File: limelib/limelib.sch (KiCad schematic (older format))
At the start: 6 parts, among them J1 ESC_CONN, SW1 SW_Push, U1 ATtiny85-20PU

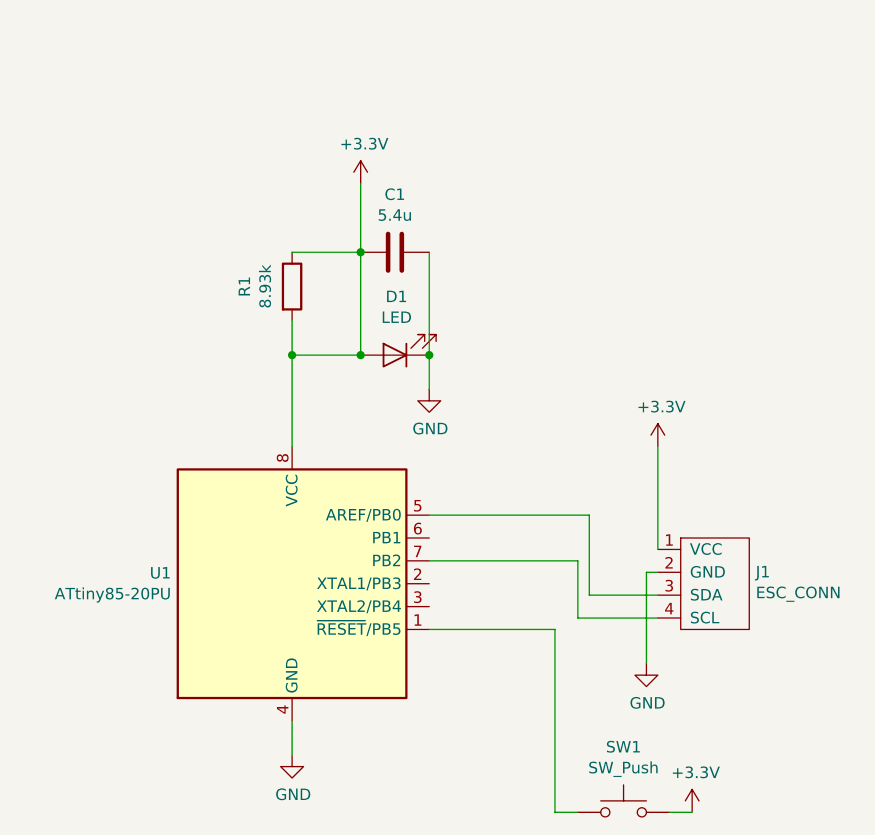
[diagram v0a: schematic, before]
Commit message: fix voltage regulator and switch
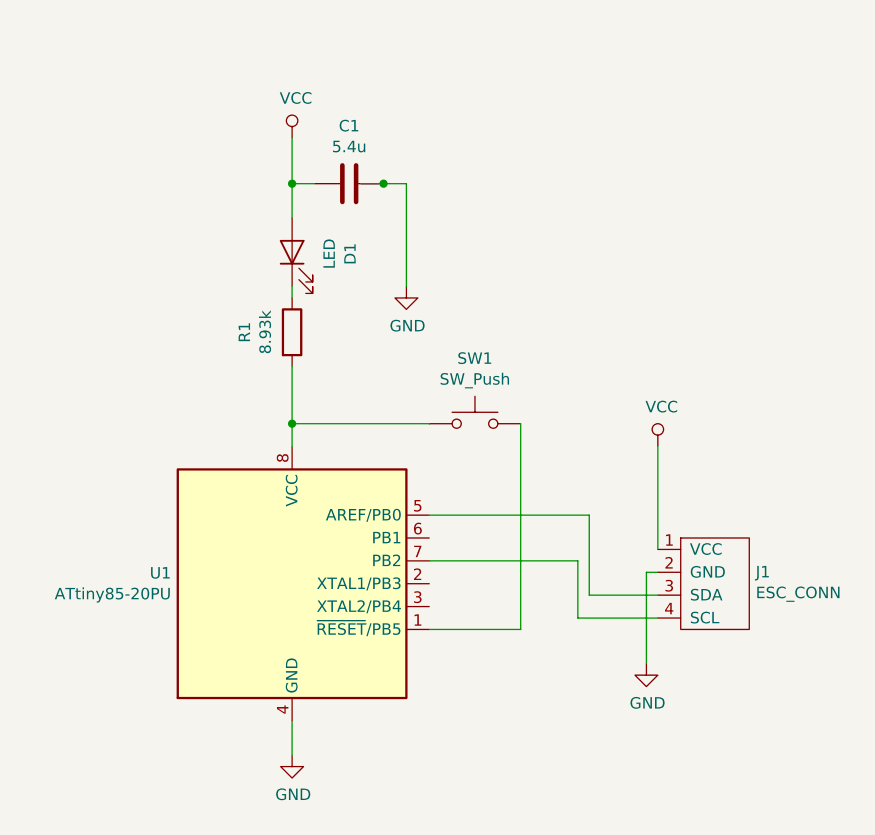
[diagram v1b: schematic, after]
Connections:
- net labels added: VCC
- net labels removed: +3.3V
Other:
- moved on the sheet: C1, D1, R1, SW1
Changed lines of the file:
@@
 EESchema Schematic File Version 4
+LIBS:limelib-cache
 EELAYER 30 0
 EELAYER END
@@
 L Device:R R1
 U 1 1 5DCA0E0D
-P 5650 2450
-F 0 "R1" V 5443 2450 50  0000 C CNN
-F 1 "8.93k" V 5534 2450 50  0000 C CNN
-F 2 "" V 5580 2450 50  0001 C CNN
-F 3 "~" H 5650 2450 50  0001 C CNN
-	1    5650 2450
+P 5650 2650
+F 0 "R1" V 5443 2650 50  0000 C CNN
+F 1 "8.93k" V 5534 2650 50  0000 C CNN
+F 2 "" V 5580 2650 50  0001 C CNN
+F 3 "~" H 5650 2650 50  0001 C CNN
+	1    5650 2650
 	1    0    0    -1
 $EndComp
@@
 L Device:C C1
 U 1 1 5DCA153E
-P 6100 2300
-F 0 "C1" V 6352 2300 50  0000 C CNN
-F 1 "5.4u" V 6261 2300 50  0000 C CNN
-F 2 "" H 6138 2150 50  0001 C CNN
-F 3 "~" H 6100 2300 50  0001 C CNN
-	1    6100 2300
+P 5900 2000
+F 0 "C1" V 6152 2000 50  0000 C CNN
+F 1 "5.4u" V 6061 2000 50  0000 C CNN
+F 2 "" H 5938 1850 50  0001 C CNN
+F 3 "~" H 5900 2000 50  0001 C CNN
+	1    5900 2000
 	0    -1   -1   0
 $EndComp
@@
 L Device:LED D1
 U 1 1 5DCA22B6
-P 6100 2750
-F 0 "D1" H 6093 2495 50  0000 C CNN
-F 1 "LED" H 6093 2586 50  0000 C CNN
-F 2 "" H 6100 2750 50  0001 C CNN
-F 3 "~" H 6100 2750 50  0001 C CNN
-	1    6100 2750
-	-1   0    0    1
+P 5650 2300
+F 0 "D1" H 5643 2045 50  0000 C CNN
+F 1 "LED" H 5643 2136 50  0000 C CNN
+F 2 "" H 5650 2300 50  0001 C CNN
+F 3 "~" H 5650 2300 50  0001 C CNN
+	1    5650 2300
+	0    -1   -1   0
 $EndComp
 $Comp
 L Switch:SW_Push SW1
 U 1 1 5DCA2F12
-P 7100 4750
-F 0 "SW1" H 7100 5035 50  0000 C CNN
-F 1 "SW_Push" H 7100 4944 50  0000 C CNN
-F 2 "" H 7100 4950 50  0001 C CNN
-F 3 "~" H 7100 4950 50  0001 C CNN
-	1    7100 4750
+P 6450 3050
+F 0 "SW1" H 6450 3335 50  0000 C CNN
+F 1 "SW_Push" H 6450 3244 50  0000 C CNN
+F 2 "" H 6450 3250 50  0001 C CNN
+F 3 "~" H 6450 3250 50  0001 C CNN
+	1    6450 3050
 	1    0    0    -1
 $EndComp
@@
 	7200 3700 7200 4100
 Wire Wire Line
-	6250 3950 6800 3950
-Wire Wire Line
-	6800 3950 6800 4750
-Wire Wire Line
-	6800 4750 6900 4750
-Wire Wire Line
-	7400 4750 7300 4750
-Wire Wire Line
 	7250 3800 6950 3800
 Wire Wire Line
@@
 L power:GND #PWR?
 U 1 1 5DCBD74A
-P 6250 2900
-F 0 "#PWR?" H 6250 2650 50  0001 C CNN
-F 1 "GND" H 6255 2727 50  0000 C CNN
-F 2 "" H 6250 2900 50  0001 C CNN
-F 3 "" H 6250 2900 50  0001 C CNN
-	1    6250 2900
+P 6150 2450
+F 0 "#PWR?" H 6150 2200 50  0001 C CNN
+F 1 "GND" H 6155 2277 50  0000 C CNN
+F 2 "" H 6150 2450 50  0001 C CNN
+F 3 "" H 6150 2450 50  0001 C CNN
+	1    6150 2450
 	1    0    0    -1
 $EndComp
 Wire Wire Line
-	5950 2300 5950 2000
-Connection ~ 5950 2300
+	7250 3150 7250 3600
+$Comp
+L power:VCC #PWR?
+U 1 1 5DCB2ABE
+P 5650 1800
+F 0 "#PWR?" H 5650 1650 50  0001 C CNN
+F 1 "VCC" H 5667 1973 50  0000 C CNN
+F 2 "" H 5650 1800 50  0001 C CNN
+F 3 "" H 5650 1800 50  0001 C CNN
+	1    5650 1800
+	1    0    0    -1
+$EndComp
 Wire Wire Line
-	5650 2600 5650 2750
+	5650 2450 5650 2500
 Wire Wire Line
-	5650 2300 5950 2300
+	5650 1800 5650 2000
+Connection ~ 5650 2000
 Wire Wire Line
-	5950 2750 5650 2750
+	5650 2000 5650 2150
 Wire Wire Line
-	5650 2750 5650 3150
-Connection ~ 5650 2750
+	6150 2000 6150 2450
+Wire Wire Line
+	5650 2000 5750 2000
+Wire Wire Line
+	5950 2000 6050 2000
 $Comp
-L power:+3.3V #PWR?
-U 1 1 5DCDEE7B
+L power:VCC #PWR?
+U 1 1 5DCBCC27
 P 7250 3150
 F 0 "#PWR?" H 7250 3000 50  0001 C CNN
-F 1 "+3.3V" H 7265 3323 50  0000 C CNN
+F 1 "VCC" H 7267 3323 50  0000 C CNN
 F 2 "" H 7250 3150 50  0001 C CNN
 F 3 "" H 7250 3150 50  0001 C CNN
@@
 	1    0    0    -1
 $EndComp
+Connection ~ 6050 2000
 Wire Wire Line
-	7250 3150 7250 3600
-$Comp
-L power:+3.3V #PWR?
-U 1 1 5DCDFD0C
-P 5950 2000
-F 0 "#PWR?" H 5950 1850 50  0001 C CNN
-F 1 "+3.3V" H 5965 2173 50  0000 C CNN
-F 2 "" H 5950 2000 50  0001 C CNN
-F 3 "" H 5950 2000 50  0001 C CNN
-	1    5950 2000
-	1    0    0    -1
-$EndComp
-$Comp
-L power:+3.3V #PWR?
-U 1 1 5DCE016F
-P 7400 4750
-F 0 "#PWR?" H 7400 4600 50  0001 C CNN
-F 1 "+3.3V" H 7415 4923 50  0000 C CNN
-F 2 "" H 7400 4750 50  0001 C CNN
-F 3 "" H 7400 4750 50  0001 C CNN
-	1    7400 4750
-	1    0    0    -1
-$EndComp
+	6050 2000 6150 2000
 Wire Wire Line
-	6250 2300 6250 2750
-Connection ~ 6250 2750
+	5650 2800 5650 3050
 Wire Wire Line
-	6250 2750 6250 2900
+	6250 3050 5650 3050
+Connection ~ 5650 3050
 Wire Wire Line
-	5950 2300 5950 2750
-Connection ~ 5950 2750
+	5650 3050 5650 3150
+Wire Wire Line
+	6650 3050 6650 3950
+Wire Wire Line
+	6650 3950 6250 3950
 $EndSCHEMATC

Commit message: another shot at the LED regulator circuit
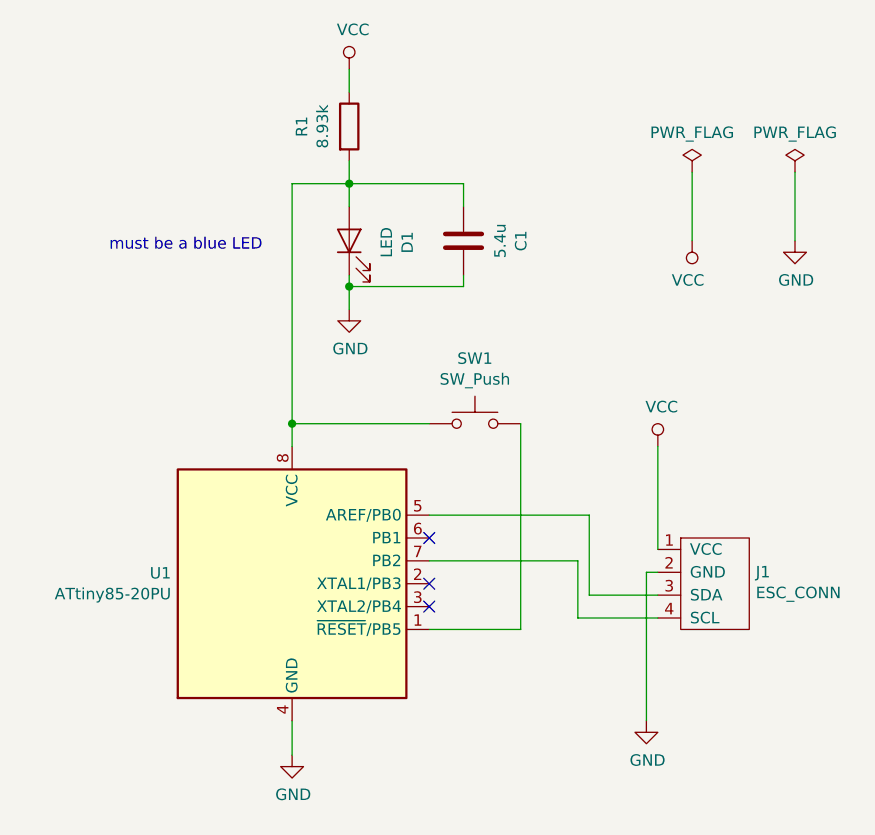
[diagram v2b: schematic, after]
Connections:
- wire segments 22 -> 27
- no-connect marks 0 -> 3
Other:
- note added: "must be a blue LED"
- moved on the sheet: C1, D1, R1
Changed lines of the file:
@@
 L Device:R R1
 U 1 1 5DCA0E0D
-P 5650 2650
-F 0 "R1" V 5443 2650 50  0000 C CNN
-F 1 "8.93k" V 5534 2650 50  0000 C CNN
-F 2 "" V 5580 2650 50  0001 C CNN
-F 3 "~" H 5650 2650 50  0001 C CNN
-	1    5650 2650
+P 5900 1750
+F 0 "R1" V 5693 1750 50  0000 C CNN
+F 1 "8.93k" V 5784 1750 50  0000 C CNN
+F 2 "" V 5830 1750 50  0001 C CNN
+F 3 "~" H 5900 1750 50  0001 C CNN
+	1    5900 1750
 	1    0    0    -1
 $EndComp
@@
 L Device:C C1
 U 1 1 5DCA153E
-P 5900 2000
-F 0 "C1" V 6152 2000 50  0000 C CNN
-F 1 "5.4u" V 6061 2000 50  0000 C CNN
-F 2 "" H 5938 1850 50  0001 C CNN
-F 3 "~" H 5900 2000 50  0001 C CNN
-	1    5900 2000
-	0    -1   -1   0
+P 6400 2250
+F 0 "C1" V 6652 2250 50  0000 C CNN
+F 1 "5.4u" V 6561 2250 50  0000 C CNN
+F 2 "" H 6438 2100 50  0001 C CNN
+F 3 "~" H 6400 2250 50  0001 C CNN
+	1    6400 2250
+	1    0    0    -1
 $EndComp
 $Comp
 L Device:LED D1
 U 1 1 5DCA22B6
-P 5650 2300
-F 0 "D1" H 5643 2045 50  0000 C CNN
-F 1 "LED" H 5643 2136 50  0000 C CNN
-F 2 "" H 5650 2300 50  0001 C CNN
-F 3 "~" H 5650 2300 50  0001 C CNN
-	1    5650 2300
+P 5900 2250
+F 0 "D1" H 5893 1995 50  0000 C CNN
+F 1 "LED" H 5893 2086 50  0000 C CNN
+F 2 "" H 5900 2250 50  0001 C CNN
+F 3 "~" H 5900 2250 50  0001 C CNN
+	1    5900 2250
 	0    -1   -1   0
 $EndComp
@@
 $EndComp
 $Comp
-L power:GND #PWR?
+L power:GND #PWR0101
 U 1 1 5DCA42A6
 P 5650 4500
-F 0 "#PWR?" H 5650 4250 50  0001 C CNN
+F 0 "#PWR0101" H 5650 4250 50  0001 C CNN
 F 1 "GND" H 5655 4327 50  0000 C CNN
 F 2 "" H 5650 4500 50  0001 C CNN
@@
 $EndComp
 $Comp
-L power:GND #PWR?
+L power:GND #PWR0102
 U 1 1 5DCADE5E
-P 7200 4100
-F 0 "#PWR?" H 7200 3850 50  0001 C CNN
-F 1 "GND" H 7205 3927 50  0000 C CNN
-F 2 "" H 7200 4100 50  0001 C CNN
-F 3 "" H 7200 4100 50  0001 C CNN
-	1    7200 4100
+P 7200 4350
+F 0 "#PWR0102" H 7200 4100 50  0001 C CNN
+F 1 "GND" H 7205 4177 50  0000 C CNN
+F 2 "" H 7200 4350 50  0001 C CNN
+F 3 "" H 7200 4350 50  0001 C CNN
+	1    7200 4350
 	1    0    0    -1
 $EndComp
@@
 	7250 3700 7200 3700
 Wire Wire Line
-	7200 3700 7200 4100
-Wire Wire Line
 	7250 3800 6950 3800
 Wire Wire Line
@@
 	6900 3650 6250 3650
 $Comp
-L power:GND #PWR?
-U 1 1 5DCBD74A
-P 6150 2450
-F 0 "#PWR?" H 6150 2200 50  0001 C CNN
-F 1 "GND" H 6155 2277 50  0000 C CNN
-F 2 "" H 6150 2450 50  0001 C CNN
-F 3 "" H 6150 2450 50  0001 C CNN
-	1    6150 2450
-	1    0    0    -1
-$EndComp
-Wire Wire Line
-	7250 3150 7250 3600
-$Comp
-L power:VCC #PWR?
+L power:VCC #PWR0104
 U 1 1 5DCB2ABE
-P 5650 1800
-F 0 "#PWR?" H 5650 1650 50  0001 C CNN
-F 1 "VCC" H 5667 1973 50  0000 C CNN
-F 2 "" H 5650 1800 50  0001 C CNN
-F 3 "" H 5650 1800 50  0001 C CNN
-	1    5650 1800
-	1    0    0    -1
-$EndComp
-Wire Wire Line
-	5650 2450 5650 2500
-Wire Wire Line
-	5650 1800 5650 2000
-Connection ~ 5650 2000
-Wire Wire Line
-	5650 2000 5650 2150
-Wire Wire Line
-	6150 2000 6150 2450
-Wire Wire Line
-	5650 2000 5750 2000
-Wire Wire Line
-	5950 2000 6050 2000
-$Comp
-L power:VCC #PWR?
+P 5900 1500
+F 0 "#PWR0104" H 5900 1350 50  0001 C CNN
+F 1 "VCC" H 5917 1673 50  0000 C CNN
+F 2 "" H 5900 1500 50  0001 C CNN
+F 3 "" H 5900 1500 50  0001 C CNN
+	1    5900 1500
+	1    0    0    -1
+$EndComp
+Wire Wire Line
+	5900 2400 5900 2450
+$Comp
+L power:VCC #PWR0105
 U 1 1 5DCBCC27
 P 7250 3150
-F 0 "#PWR?" H 7250 3000 50  0001 C CNN
+F 0 "#PWR0105" H 7250 3000 50  0001 C CNN
 F 1 "VCC" H 7267 3323 50  0000 C CNN
 F 2 "" H 7250 3150 50  0001 C CNN
@@
 	1    0    0    -1
 $EndComp
-Connection ~ 6050 2000
-Wire Wire Line
-	6050 2000 6150 2000
-Wire Wire Line
-	5650 2800 5650 3050
 Wire Wire Line
 	6250 3050 5650 3050
+Wire Wire Line
+	5650 3050 5650 3150
+Wire Wire Line
+	6650 3050 6650 3950
+Wire Wire Line
+	6650 3950 6250 3950
+NoConn ~ 6250 3550
+NoConn ~ 6250 3750
+NoConn ~ 6250 3850
+Text Notes 4850 2300 0    50   ~ 0
+must be a blue LED
+Wire Wire Line
+	7250 3150 7250 3600
+Wire Wire Line
+	7200 3700 7200 4350
+$Comp
+L power:VCC #PWR0106
+U 1 1 5DCCD262
+P 7400 2250
+F 0 "#PWR0106" H 7400 2100 50  0001 C CNN
+F 1 "VCC" H 7418 2423 50  0000 C CNN
+F 2 "" H 7400 2250 50  0001 C CNN
+F 3 "" H 7400 2250 50  0001 C CNN
+	1    7400 2250
+	-1   0    0    1
+$EndComp
+$Comp
+L power:PWR_FLAG #FLG0101
+U 1 1 5DCCD779
+P 7400 1950
+F 0 "#FLG0101" H 7400 2025 50  0001 C CNN
+F 1 "PWR_FLAG" H 7400 2123 50  0000 C CNN
+F 2 "" H 7400 1950 50  0001 C CNN
+F 3 "~" H 7400 1950 50  0001 C CNN
+	1    7400 1950
+	1    0    0    -1
+$EndComp
+Wire Wire Line
+	7400 1950 7400 2250
+$Comp
+L power:GND #PWR0107
+U 1 1 5DCCDEC2
+P 7850 2250
+F 0 "#PWR0107" H 7850 2000 50  0001 C CNN
+F 1 "GND" H 7855 2077 50  0000 C CNN
+F 2 "" H 7850 2250 50  0001 C CNN
+F 3 "" H 7850 2250 50  0001 C CNN
+	1    7850 2250
+	1    0    0    -1
+$EndComp
+$Comp
+L power:PWR_FLAG #FLG0102
+U 1 1 5DCCE3B4
+P 7850 1950
+F 0 "#FLG0102" H 7850 2025 50  0001 C CNN
+F 1 "PWR_FLAG" H 7850 2123 50  0000 C CNN
+F 2 "" H 7850 1950 50  0001 C CNN
+F 3 "~" H 7850 1950 50  0001 C CNN
+	1    7850 1950
+	1    0    0    -1
+$EndComp
+Wire Wire Line
+	7850 1950 7850 2250
+Wire Wire Line
+	6400 2100 6400 2000
+Wire Wire Line
+	6400 2000 5900 2000
+Wire Wire Line
+	5900 2000 5900 2100
+Wire Wire Line
+	6400 2400 6400 2450
+Wire Wire Line
+	6400 2450 5900 2450
+Wire Wire Line
+	5900 1900 5900 2000
+Connection ~ 5900 2000
+Wire Wire Line
+	5900 1500 5900 1600
+Wire Wire Line
+	5900 2000 5650 2000
+Wire Wire Line
+	5650 2000 5650 3050
 Connection ~ 5650 3050
-Wire Wire Line
-	5650 3050 5650 3150
-Wire Wire Line
-	6650 3050 6650 3950
-Wire Wire Line
-	6650 3950 6250 3950
+$Comp
+L power:GND #PWR0103
+U 1 1 5DCBF729
+P 5900 2550
+F 0 "#PWR0103" H 5900 2300 50  0001 C CNN
+F 1 "GND" H 5905 2377 50  0000 C CNN
+F 2 "" H 5900 2550 50  0001 C CNN
+F 3 "" H 5900 2550 50  0001 C CNN
+	1    5900 2550
+	1    0    0    -1
+$EndComp
+Wire Wire Line
+	5900 2550 5900 2450
+Connection ~ 5900 2450
 $EndSCHEMATC
